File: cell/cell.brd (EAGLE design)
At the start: 35.5 x 48.3 mm, 11 parts

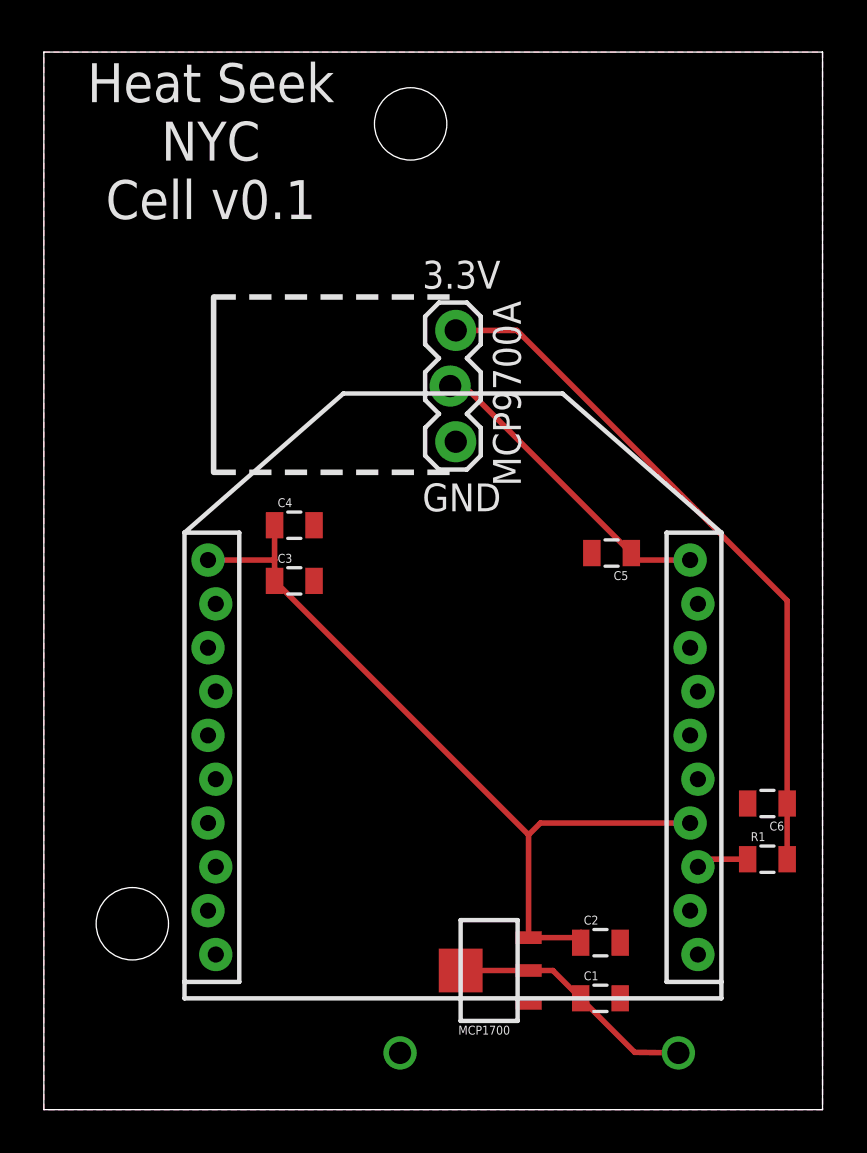
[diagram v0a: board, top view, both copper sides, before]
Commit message: cell v0.2, with on-board temperature sensor and better layout
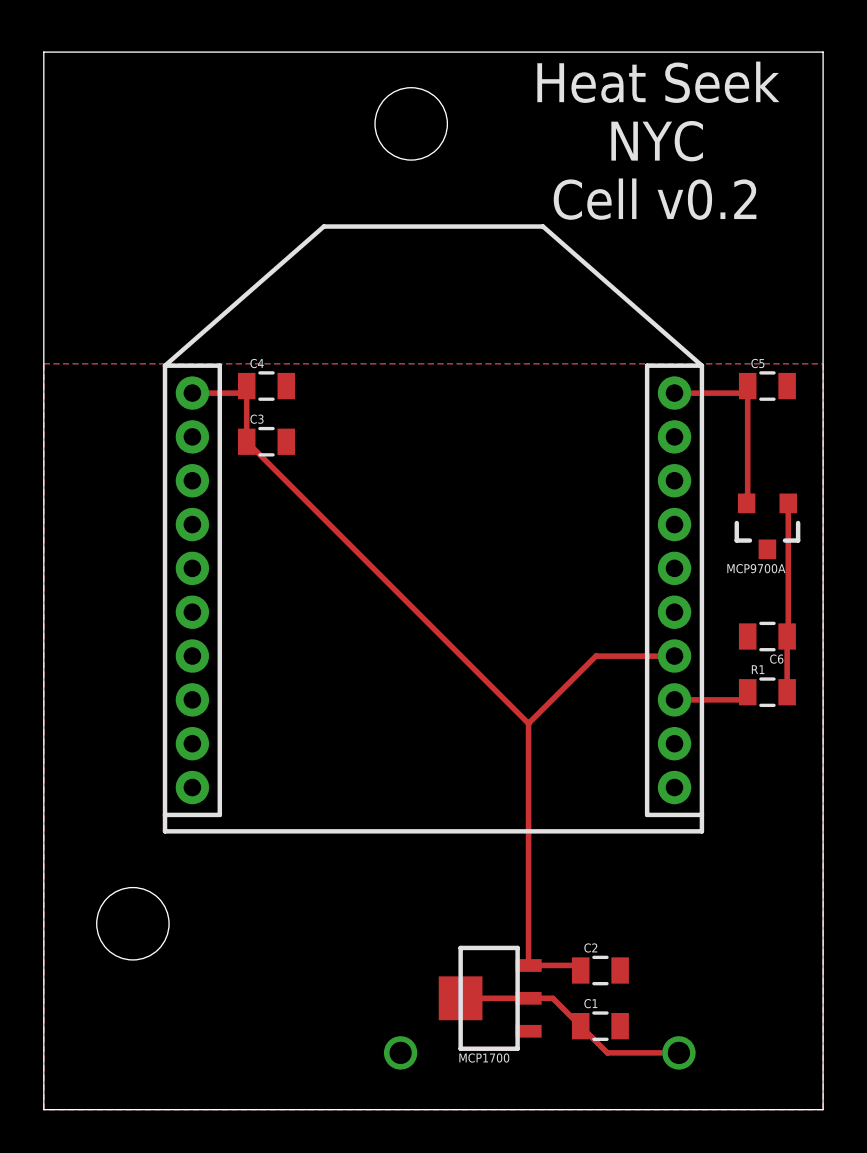
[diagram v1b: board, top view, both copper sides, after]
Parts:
- MCP9700A: value (none) -> MCP9700SMD; device SparkFun-Connectors:1X03_LOCK -> SparkFun-Sensors:SOT23-3
- XB24: value XBEE-1XBEE-1_LOCK -> XBEE-1XBEE-1; device hrldcpr:XBEE-1_LOCK -> hrldcpr:XBEE-1
- moved MCP9700A 16.9 mm to (33.0, 26.7), turned to 180 degrees
- moved C5 10.4 mm to (33.0, 33.0), turned to 0 degrees
- moved XB24 7.67 mm to (17.8, 12.7)
- moved R1 7.62 mm to (33.0, 19.1)
- moved C6 7.62 mm to (33.0, 21.6)
- moved C3 6.48 mm to (10.2, 30.5)
- moved C4 6.48 mm to (10.2, 33.0)
- moved C2 1.27 mm to (25.4, 6.35)
- moved C1 1.27 mm to (25.4, 3.81)
- moved MCP1700 1.27 mm to (20.3, 5.08)
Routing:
- net N$1: track 32.0 -> 8.67 mm
- net 3.3V: track 37.1 -> 45.1 mm
- net N$3: track 14.4 -> 9.06 mm
- net N$5: track 0.00 -> 2.54 mm
- net N$4: track 2.54 -> 0.00 mm
- net N$2: track 2.42 -> 3.69 mm
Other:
- board size 35.5 x 48.3 mm -> 35.6 x 48.3 mm
- board text added: "Heat Seek NYC Cell v0.2"
- board text removed: "3.3V"
- board text removed: "GND"
- board text removed: "Heat Seek NYC Cell v0.1"
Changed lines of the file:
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@@
 <board>
 <plain>
-<wire x1="0" y1="0" x2="35.5346" y2="0" width="0" layer="20"/>
-<wire x1="35.5346" y1="0" x2="35.5346" y2="48.26" width="0" layer="20"/>
-<wire x1="35.5346" y1="48.26" x2="0" y2="48.26" width="0" layer="20"/>
+<wire x1="0" y1="0" x2="35.56" y2="0" width="0" layer="20"/>
+<wire x1="35.56" y1="0" x2="35.56" y2="48.26" width="0" layer="20"/>
+<wire x1="35.56" y1="48.26" x2="0" y2="48.26" width="0" layer="20"/>
 <wire x1="0" y1="48.26" x2="0" y2="0" width="0" layer="20"/>
-<hole x="4.0386" y="8.4836" drill="3.302"/>
-<hole x="16.7386" y="44.9834" drill="3.302"/>
-<text x="7.62" y="40.64" size="1.778" layer="21" font="vector" ratio="15" align="bottom-center">Heat Seek
+<hole x="4.064" y="8.4836" drill="3.302"/>
+<hole x="16.764" y="44.9834" drill="3.302"/>
+<text x="27.94" y="40.64" size="1.778" layer="21" font="vector" ratio="15" align="bottom-center">Heat Seek
 NYC
-Cell v0.1</text>
+Cell v0.2</text>
 <text x="26.67" y="59.69" size="1.778" layer="51" font="vector" ratio="15">Harold Cooper</text>
-<wire x1="7.747" y1="29.083" x2="7.747" y2="37.084" width="0.254" layer="21"/>
-<wire x1="7.747" y1="37.084" x2="18.669" y2="37.084" width="0.254" layer="21" style="shortdash"/>
-<wire x1="7.747" y1="29.083" x2="18.669" y2="29.083" width="0.254" layer="21" style="shortdash"/>
-<text x="17.272" y="38.1" size="1.27" layer="21" font="vector" ratio="15" align="center-left">3.3V</text>
-<text x="17.272" y="27.94" size="1.27" layer="21" font="vector" ratio="15" align="center-left">GND</text>
 </plain>
 <attributes>
@@
 <elements>
 <element name="FRAME1" library="SparkFun-Aesthetics" package="CREATIVE_COMMONS" value="FRAME-LETTER" x="0" y="60"/>
-<element name="C1" library="SparkFun-Capacitors" package="0805" value="1µF" x="25.4" y="5.08"/>
-<element name="C3" library="SparkFun-Capacitors" package="0805" value="1µF" x="11.43" y="24.13"/>
-<element name="C4" library="SparkFun-Capacitors" package="0805" value="8.2pF" x="11.43" y="26.67"/>
-<element name="C5" library="SparkFun-Capacitors" package="0805" value="0.1µF" x="25.908" y="25.4" rot="R180"/>
-<element name="C6" library="SparkFun-Capacitors" package="0805" value="1µF" x="33.02" y="13.97" rot="R180"/>
-<element name="R1" library="SparkFun-Resistors" package="0805" value="200Ω" x="33.02" y="11.43"/>
-<element name="XB24" library="hrldcpr" package="XBEE-1_LOCK" value="XBEE-1XBEE-1_LOCK" x="18.669" y="5.08"/>
-<element name="MCP1700" library="hrldcpr" package="SOT-89-3" value="MCP1700" x="20.32" y="6.35" rot="R90"/>
-<element name="C2" library="SparkFun-Capacitors" package="0805" value="1µF" x="25.4" y="7.62"/>
-<element name="MCP9700A" library="SparkFun-Connectors" package="1X03_LOCK" value="" x="18.669" y="35.56" rot="R270"/>
+<element name="C1" library="SparkFun-Capacitors" package="0805" value="1µF" x="25.4" y="3.81"/>
+<element name="C3" library="SparkFun-Capacitors" package="0805" value="1µF" x="10.16" y="30.48"/>
+<element name="C4" library="SparkFun-Capacitors" package="0805" value="8.2pF" x="10.16" y="33.02"/>
+<element name="C5" library="SparkFun-Capacitors" package="0805" value="0.1µF" x="33.02" y="33.02"/>
+<element name="C6" library="SparkFun-Capacitors" package="0805" value="1µF" x="33.02" y="21.59" rot="R180"/>
+<element name="R1" library="SparkFun-Resistors" package="0805" value="200Ω" x="33.02" y="19.05"/>
+<element name="MCP1700" library="hrldcpr" package="SOT-89-3" value="MCP1700" x="20.32" y="5.08" rot="R90"/>
+<element name="C2" library="SparkFun-Capacitors" package="0805" value="1µF" x="25.4" y="6.35"/>
+<element name="MCP9700A" library="SparkFun-Sensors" package="SOT23-3" value="MCP9700SMD" x="33.02" y="26.67" rot="R180">
+<attribute name="PROD_ID" value="IC-08917" x="33.02" y="26.67" size="1.778" layer="27" rot="R180" display="off"/>
+</element>
+<element name="XB24" library="hrldcpr" package="XBEE-1" value="XBEE-1XBEE-1" x="17.78" y="12.7"/>
 </elements>
 <signals>
@@
 <polygon width="0.254" layer="16">
 <vertex x="0" y="0"/>
-<vertex x="0" y="48.26"/>
-<vertex x="35.5346" y="48.26"/>
-<vertex x="35.5346" y="0"/>
+<vertex x="0" y="34.036"/>
+<vertex x="35.56" y="34.036"/>
+<vertex x="35.56" y="0"/>
 </polygon>
 <polygon width="0.254" layer="1">
 <vertex x="0" y="0"/>
-<vertex x="0" y="48.26"/>
-<vertex x="35.5346" y="48.26"/>
-<vertex x="35.5346" y="0"/>
+<vertex x="0" y="34.036"/>
+<vertex x="35.56" y="34.036"/>
+<vertex x="35.56" y="0"/>
 </polygon>
-<via x="16.256" y="2.5908" extent="1-16" drill="1.016"/>
-<contactref element="XB24" pad="10"/>
+<via x="16.2814" y="2.5908" extent="1-16" drill="1.016"/>
 <contactref element="MCP1700" pad="1"/>
 <contactref element="C2" pad="2"/>
 <contactref element="MCP9700A" pad="3"/>
+<contactref element="XB24" pad="10"/>
 </signal>
 <signal name="V_BATT">
 <contactref element="C1" pad="1"/>
 <contactref element="C1" pad="1"/>
-<via x="28.956" y="2.5908" extent="1-16" drill="1.016"/>
+<via x="28.9814" y="2.5908" extent="1-16" drill="1.016"/>
 <contactref element="MCP1700" pad="2"/>
-<wire x1="22.12" y1="6.35" x2="23.23" y2="6.35" width="0.254" layer="1"/>
-<wire x1="23.23" y1="6.35" x2="24.5" y2="5.08" width="0.254" layer="1"/>
-<wire x1="24.5" y1="5.08" x2="26.9638" y2="2.6162" width="0.254" layer="1"/>
-<wire x1="26.9638" y1="2.6162" x2="28.956" y2="2.5908" width="0.254" layer="1"/>
+<wire x1="24.5" y1="3.81" x2="25.7192" y2="2.5908" width="0.254" layer="1"/>
+<wire x1="25.7192" y1="2.5908" x2="28.9814" y2="2.5908" width="0.254" layer="1"/>
+<wire x1="24.5" y1="3.81" x2="23.23" y2="5.08" width="0.254" layer="1"/>
+<wire x1="23.23" y1="5.08" x2="22.12" y2="5.08" width="0.254" layer="1"/>
 </signal>
 <signal name="3.3V">
 <contactref element="C3" pad="1"/>
 <contactref element="C4" pad="1"/>
+<contactref element="C2" pad="1"/>
+<contactref element="MCP1700" pad="3"/>
+<wire x1="9.26" y1="33.02" x2="9.26" y2="30.48" width="0.254" layer="1"/>
 <contactref element="XB24" pad="1"/>
 <contactref element="XB24" pad="14"/>
-<contactref element="C2" pad="1"/>
-<contactref element="MCP1700" pad="3"/>
-<wire x1="7.4912" y1="25.08" x2="10.53" y2="25.08" width="0.254" layer="1"/>
-<wire x1="10.53" y1="25.08" x2="10.53" y2="26.67" width="0.254" layer="1"/>
-<wire x1="10.53" y1="25.08" x2="10.53" y2="24.13" width="0.254" layer="1"/>
-<wire x1="24.5" y1="8.0888" x2="24.5" y2="7.85" width="0.254" layer="1"/>
-<wire x1="24.5" y1="7.85" x2="24.5" y2="7.62" width="0.254" layer="1"/>
-<wire x1="24.5" y1="7.85" x2="22.12" y2="7.85" width="0.254" layer="1"/>
-<wire x1="22.12" y1="7.85" x2="22.12" y2="12.54" width="0.254" layer="1"/>
-<wire x1="22.12" y1="12.54" x2="10.53" y2="24.13" width="0.254" layer="1"/>
-<wire x1="29.4912" y1="13.08" x2="22.66" y2="13.08" width="0.254" layer="1"/>
-<wire x1="22.66" y1="13.08" x2="22.12" y2="12.54" width="0.254" layer="1"/>
+<wire x1="22.12" y1="6.58" x2="24.5" y2="6.58" width="0.254" layer="1"/>
+<wire x1="24.5" y1="6.58" x2="24.5" y2="6.35" width="0.254" layer="1"/>
+<wire x1="6.78" y1="32.7" x2="9.26" y2="32.7" width="0.254" layer="1"/>
+<wire x1="9.26" y1="32.7" x2="9.26" y2="33.02" width="0.254" layer="1"/>
+<wire x1="22.12" y1="6.58" x2="22.12" y2="17.62" width="0.254" layer="1"/>
+<wire x1="22.12" y1="17.62" x2="9.26" y2="30.48" width="0.254" layer="1"/>
+<wire x1="28.78" y1="20.7" x2="25.2" y2="20.7" width="0.254" layer="1"/>
+<wire x1="25.2" y1="20.7" x2="22.12" y2="17.62" width="0.254" layer="1"/>
 </signal>
 <signal name="N$1">
@@
 <contactref element="R1" pad="2"/>
 <contactref element="MCP9700A" pad="1"/>
-<wire x1="33.92" y1="13.97" x2="33.92" y2="11.43" width="0.254" layer="1"/>
-<wire x1="33.92" y1="13.97" x2="33.92" y2="23.23" width="0.254" layer="1"/>
-<wire x1="33.92" y1="23.23" x2="21.59" y2="35.56" width="0.254" layer="1"/>
-<wire x1="21.59" y1="35.56" x2="18.796" y2="35.56" width="0.254" layer="1"/>
+<contactref element="MCP9700A" pad="1"/>
+<wire x1="33.92" y1="19.05" x2="33.92" y2="21.59" width="0.254" layer="1"/>
+<wire x1="33.92" y1="21.59" x2="33.97" y2="21.59" width="0.254" layer="1"/>
+<wire x1="33.97" y1="21.59" x2="33.97" y2="27.67" width="0.254" layer="1"/>
 </signal>
 <signal name="N$2">
 <contactref element="R1" pad="1"/>
 <contactref element="XB24" pad="13"/>
-<wire x1="32.12" y1="11.43" x2="30.1968" y2="11.43" width="0.254" layer="1"/>
-<wire x1="30.1968" y1="11.43" x2="29.8468" y2="11.08" width="0.254" layer="1"/>
+<wire x1="28.78" y1="18.7" x2="32.12" y2="18.7" width="0.254" layer="1"/>
+<wire x1="32.12" y1="18.7" x2="32.12" y2="19.05" width="0.254" layer="1"/>
 </signal>
 <signal name="N$3">
 <contactref element="C5" pad="1"/>
+<contactref element="MCP9700A" pad="2"/>
 <contactref element="XB24" pad="20"/>
-<contactref element="MCP9700A" pad="2"/>
-<wire x1="26.808" y1="25.4" x2="26.808" y2="25.08" width="0.254" layer="1"/>
-<wire x1="26.808" y1="25.08" x2="29.4912" y2="25.08" width="0.254" layer="1"/>
-<wire x1="26.808" y1="25.4" x2="19.188" y2="33.02" width="0.254" layer="1"/>
-<wire x1="19.188" y1="33.02" x2="18.542" y2="33.02" width="0.254" layer="1"/>
+<wire x1="32.07" y1="27.67" x2="32.12" y2="27.67" width="0.254" layer="1"/>
+<wire x1="32.12" y1="27.67" x2="32.12" y2="33.02" width="0.254" layer="1"/>
+<wire x1="28.78" y1="32.7" x2="32.12" y2="32.7" width="0.254" layer="1"/>
+<wire x1="32.12" y1="32.7" x2="32.12" y2="33.02" width="0.254" layer="1"/>
 </signal>
 <signal name="N$4">
-<wire x1="21.59" y1="6.35" x2="19.05" y2="6.35" width="0.254" layer="1"/>
+</signal>
+<signal name="N$5">
+<wire x1="21.59" y1="5.08" x2="19.05" y2="5.08" width="0.254" layer="1"/>
 </signal>
 </signals>

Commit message: cell v0.3, with power plane eliminating the major traces
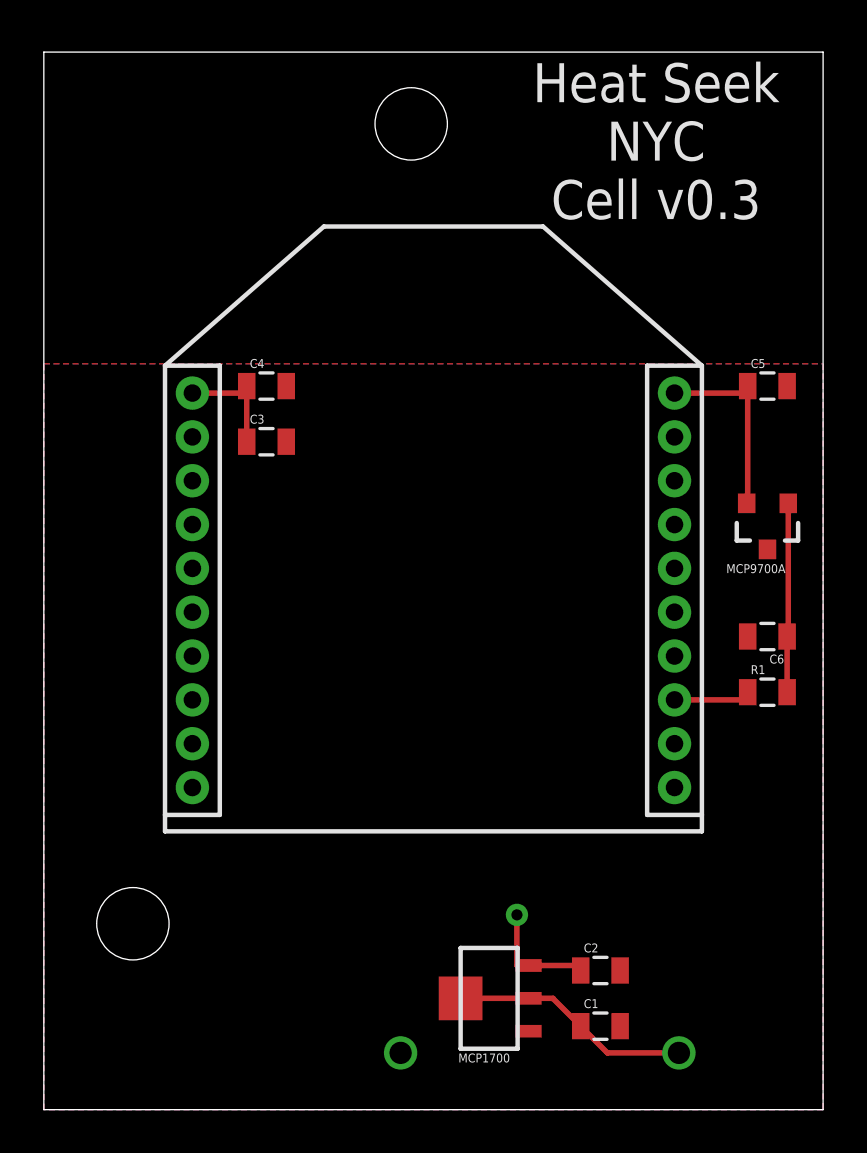
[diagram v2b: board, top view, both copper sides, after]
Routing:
- net 3.3V: track 45.1 -> 10.8 mm, vias 0 -> 1
- added copper zone on layer 16, net 3.3V
- removed copper zone on layer 16, net GND
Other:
- board text added: "Heat Seek NYC Cell v0.3"
- board text removed: "Heat Seek NYC Cell v0.2"
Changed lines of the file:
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@@
 <text x="27.94" y="40.64" size="1.778" layer="21" font="vector" ratio="15" align="bottom-center">Heat Seek
 NYC
-Cell v0.2</text>
+Cell v0.3</text>
 <text x="26.67" y="59.69" size="1.778" layer="51" font="vector" ratio="15">Harold Cooper</text>
 </plain>
@@
 <contactref element="C1" pad="2"/>
 <contactref element="C4" pad="2"/>
-<polygon width="0.254" layer="16">
-<vertex x="0" y="0"/>
-<vertex x="0" y="34.036"/>
-<vertex x="35.56" y="34.036"/>
-<vertex x="35.56" y="0"/>
-</polygon>
 <polygon width="0.254" layer="1">
 <vertex x="0" y="0"/>
@@
 <contactref element="XB24" pad="1"/>
 <contactref element="XB24" pad="14"/>
-<wire x1="22.12" y1="6.58" x2="24.5" y2="6.58" width="0.254" layer="1"/>
 <wire x1="24.5" y1="6.58" x2="24.5" y2="6.35" width="0.254" layer="1"/>
 <wire x1="6.78" y1="32.7" x2="9.26" y2="32.7" width="0.254" layer="1"/>
 <wire x1="9.26" y1="32.7" x2="9.26" y2="33.02" width="0.254" layer="1"/>
-<wire x1="22.12" y1="6.58" x2="22.12" y2="17.62" width="0.254" layer="1"/>
-<wire x1="22.12" y1="17.62" x2="9.26" y2="30.48" width="0.254" layer="1"/>
-<wire x1="28.78" y1="20.7" x2="25.2" y2="20.7" width="0.254" layer="1"/>
-<wire x1="25.2" y1="20.7" x2="22.12" y2="17.62" width="0.254" layer="1"/>
+<polygon width="0.254" layer="16">
+<vertex x="0" y="0"/>
+<vertex x="0" y="34.036"/>
+<vertex x="35.56" y="34.036"/>
+<vertex x="35.56" y="0"/>
+</polygon>
+<via x="21.59" y="8.89" extent="1-16" drill="0.508"/>
+<wire x1="24.5" y1="6.58" x2="22.12" y2="6.58" width="0.254" layer="1"/>
+<wire x1="21.59" y1="8.89" x2="21.59" y2="6.58" width="0.254" layer="1"/>
+<wire x1="21.59" y1="6.58" x2="22.12" y2="6.58" width="0.254" layer="1"/>
 </signal>
 <signal name="N$1">
